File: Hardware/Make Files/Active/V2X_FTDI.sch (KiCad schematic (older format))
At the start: 27 parts, among them P5 USB_u, U12 FT4232H, U14 93C46, X1 12M

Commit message: Saving V1.1 as archive.
We are trying a new architecture where the FTDI can be removed. making a
backup spot
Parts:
- removed C30, C32, C33, C34, C35, C36, C37, C38, C39, C40: 100N, Capacitors_SMD:C_0603, symbol C
- removed C31: 4U7, Capacitors_SMD:C_0805, symbol CP1
- removed FB6: 220, Capacitors_SMD:C_0805, symbol FILTER
- removed P5: USB_u, Connect:USB_Micro-B, symbol USB_OTG
- removed R3: DNS, Resistors_SMD:R_0603, symbol R
- added C?: 4U7, Capacitors_SMD:C_0805, symbol CP1
- added C? (x10): 100N, Capacitors_SMD:C_0603, symbol C
- added FB?: 220, Capacitors_SMD:C_0805, symbol FILTER
- added R?: DNS, Resistors_SMD:R_0603, symbol R
- added R?: 0, Resistors_SMD:R_0603, symbol R
- C1: renamed from C28; Mouse PN (none) -> 810-C1608X7R1E104K
- C2: renamed from C29; Mouse PN (none) -> 963-LMK212B7475KG-T
- FB1: renamed from FB5; Mouse PN (none) -> 810-MPZ1608S221ATA00
- U1: renamed from U12; Mouse PN (none) -> 895-FT4232HL
- renumbered C54 to C14, C55 to C15, R54 to R1, R59 to R2, R60 to R3, R61 to R4, R62 to R5, U14 to U2
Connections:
- net labels added: ACCEL_RXD, ACCEL_TXD, CAN_RXD_FTDI, CAN_TXD, FTDI_DM, FTDI_DP, HUB_PWR_PRT1, PC_RXD, PC_TXD
- net labels removed: 5V0_OUT, ACL_CS, ACL_EN, ACL_INT1, ACL_INT2, ACL_SCK, ACL_SDI, ACL_SDO, GPRS_EN, GPRS_RESET, PB0, PB1, PD0, PD1, PD2, PD3, SIMCARD, UART_RXD, UART_TXD, USB_M, USB_P
- wire segments 64 -> 54
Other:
- note added: "Serial channel for Accelerometer data\n"
- note added: "Serial channel for OBD interface control\n"
- note added: "Serial channel for Power Sequencer control\n"
- note added: "Theory:\nThe hub will activate the FTDI\nas the USB port becomes available\nAlternately, PWRSEQ could control directly"
- note removed: "4V1_EN\nACL_EN_ALT\nOBD-SLEEP\nODB_RESET\nSIM CARD DETECT\nRING INDICATOR FROM GSM\nGSM ENABLE\nGSM RESET\n"
- note removed: "HOST Data Connection"
- note removed: "SCK\nDO\nDI\nCS\nGPIO0\nGPIO1\nGPIO2\nGPIO3"
- moved on the sheet: C14, C15, R1, U1

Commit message: V1.2 mostly done
BOM is integrated and creates mouser orders
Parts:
- removed C14, C15: 18P, Capacitors_SMD:C_0603, symbol C
- removed C2, C?: 4U7, Capacitors_SMD:C_0805, symbol CP1
- removed C? (x10): 100N, Capacitors_SMD:C_0603, symbol C
- removed R3, R4: 10K, Resistors_SMD:R_0603, symbol R
- removed R?: DNS, Resistors_SMD:R_0603, symbol R
- added C10, C11, C12, C13, C2, C4, C5, C6, C7, C8, C9: 100N, Capacitors_SMD:C_0603, symbol C
- added C3: 4U7, Capacitors_SMD:C_0603, symbol C
- added R6: 10K, Resistors_SMD:R_0603, symbol R
- added R7: 22K, Resistors_SMD:R_0603, symbol R
- added R?: 0, Resistors_SMD:R_0603, symbol R
- C1: value 100N -> 4U7; Mouse PN 810-C1608X7R1E104K -> 963-LMK212B7475KG-T
- R1: footprint Resistors_SMD:R_0603 -> (none); Mouse PN (none) -> 71-CRCW0603-12K-E3
- R3: renamed from R?; value 0 -> DNS
- R4: renamed from R2; Mouse PN (none) -> 71-CRCW0603-10K-E3
- R5: value 22K -> 10K; Mouse PN (none) -> 71-CRCW0603-10K-E3
- U2: Mouse PN (none) -> 579-93LC46BISN
- X1: value 12M -> 12MHz; symbol Crystal_Small -> CRYSTAL_SMD; Mouse PN (none) -> 815-AWSCR-12.00CV-T
- gave numbers to parts that had none: 1
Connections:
- net labels added: 3V3_B, SEQ_RXD, SEQ_TXD, ~FTDI_RESET
- net labels removed: 3V3, FTDI_RESET, PC_RXD, PC_TXD
- wire segments 54 -> 53

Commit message: V2X v1.2 sch and bom
Made changes to the schematic to V1.2 (remove FTDI possibly) and
integrade the BOM information into the sch
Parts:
- gave numbers to parts that had none: 1
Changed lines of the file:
@@
 TXD\nRXD\n~RTS\n~CTS\n~DTR\n~DSR\n~DCD\n~RI
 $Comp
-L GND #PWR01
+L GND #PWR16
 U 1 1 55AD7D06
 P 7700 4950
-F 0 "#PWR01" H 7700 4700 50  0001 C CNN
+F 0 "#PWR16" H 7700 4700 50  0001 C CNN
 F 1 "GND" V 7700 4750 50  0000 C CNN
 F 2 "" H 7700 4950 60  0000 C CNN
@@
 $EndComp
 $Comp
-L GND #PWR02
+L GND #PWR17
 U 1 1 55AD7D39
 P 5600 5050
-F 0 "#PWR02" H 5600 4800 50  0001 C CNN
+F 0 "#PWR17" H 5600 4800 50  0001 C CNN
 F 1 "GND" V 5600 4850 50  0000 C CNN
 F 2 "" H 5600 5050 60  0000 C CNN
@@
 $EndComp
 $Comp
-L GND #PWR03
+L GND #PWR11
 U 1 1 55AD8749
 P 1200 3650
-F 0 "#PWR03" H 1200 3400 50  0001 C CNN
+F 0 "#PWR11" H 1200 3400 50  0001 C CNN
 F 1 "GND" H 1200 3500 50  0000 C CNN
 F 2 "" H 1200 3650 60  0000 C CNN
@@
 $EndComp
 $Comp
-L GND #PWR04
+L GND #PWR1
 U 1 1 55AD885E
 P 1700 1250
-F 0 "#PWR04" H 1700 1000 50  0001 C CNN
+F 0 "#PWR1" H 1700 1000 50  0001 C CNN
 F 1 "GND" H 1700 1100 50  0000 C CNN
 F 2 "" H 1700 1250 60  0000 C CNN
@@
 $EndComp
 $Comp
-L GND #PWR05
+L GND #PWR3
 U 1 1 55AD8999
 P 1700 2100
-F 0 "#PWR05" H 1700 1850 50  0001 C CNN
+F 0 "#PWR3" H 1700 1850 50  0001 C CNN
 F 1 "GND" H 1700 1950 50  0000 C CNN
 F 2 "" H 1700 2100 60  0000 C CNN
@@
 $EndComp
 $Comp
-L GND #PWR06
+L GND #PWR5
 U 1 1 55AD8CCE
 P 1050 2850
-F 0 "#PWR06" H 1050 2600 50  0001 C CNN
+F 0 "#PWR5" H 1050 2600 50  0001 C CNN
 F 1 "GND" H 1050 2700 50  0000 C CNN
 F 2 "" H 1050 2850 60  0000 C CNN
@@
 Power Filtering
 $Comp
-L GND #PWR07
+L GND #PWR10
 U 1 1 55AD97DA
 P 5200 3050
-F 0 "#PWR07" H 5200 2800 50  0001 C CNN
+F 0 "#PWR10" H 5200 2800 50  0001 C CNN
 F 1 "GND" V 5200 2850 50  0000 C CNN
 F 2 "" H 5200 3050 60  0000 C CNN
@@
 $EndComp
 $Comp
-L GND #PWR08
+L GND #PWR15
 U 1 1 55AD9B20
 P 5700 3750
-F 0 "#PWR08" H 5700 3500 50  0001 C CNN
+F 0 "#PWR15" H 5700 3500 50  0001 C CNN
 F 1 "GND" H 5700 3600 50  0000 C CNN
 F 2 "" H 5700 3750 60  0000 C CNN
@@
 EECLK
 $Comp
-L GND #PWR09
+L GND #PWR19
 U 1 1 55ADAE78
 P 1550 7500
-F 0 "#PWR09" H 1550 7250 50  0001 C CNN
+F 0 "#PWR19" H 1550 7250 50  0001 C CNN
 F 1 "GND" V 1550 7300 50  0000 C CNN
 F 2 "" H 1550 7500 60  0000 C CNN
@@
 FTDI Device Configuration EEPROM
 $Comp
-L GND #PWR010
+L GND #PWR2
 U 1 1 55ADBFB3
 P 1950 1250
-F 0 "#PWR010" H 1950 1000 50  0001 C CNN
+F 0 "#PWR2" H 1950 1000 50  0001 C CNN
 F 1 "GND" H 1950 1100 50  0000 C CNN
 F 2 "" H 1950 1250 60  0000 C CNN
@@
 $EndComp
 $Comp
-L GND #PWR011
+L GND #PWR4
 U 1 1 55ADBFF1
 P 1950 2100
-F 0 "#PWR011" H 1950 1850 50  0001 C CNN
+F 0 "#PWR4" H 1950 1850 50  0001 C CNN
 F 1 "GND" H 1950 1950 50  0000 C CNN
 F 2 "" H 1950 2100 60  0000 C CNN
@@
 $EndComp
 $Comp
-L GND #PWR012
+L GND #PWR12
 U 1 1 55ADC2B9
 P 1500 3650
-F 0 "#PWR012" H 1500 3400 50  0001 C CNN
+F 0 "#PWR12" H 1500 3400 50  0001 C CNN
 F 1 "GND" H 1500 3500 50  0000 C CNN
 F 2 "" H 1500 3650 60  0000 C CNN
@@
 $EndComp
 $Comp
-L GND #PWR013
+L GND #PWR6
 U 1 1 55ADC2C5
 P 1350 2850
-F 0 "#PWR013" H 1350 2600 50  0001 C CNN
+F 0 "#PWR6" H 1350 2600 50  0001 C CNN
 F 1 "GND" H 1350 2700 50  0000 C CNN
 F 2 "" H 1350 2850 60  0000 C CNN
@@
 $EndComp
 $Comp
-L GND #PWR014
+L GND #PWR13
 U 1 1 55ADC34F
 P 1800 3650
-F 0 "#PWR014" H 1800 3400 50  0001 C CNN
+F 0 "#PWR13" H 1800 3400 50  0001 C CNN
 F 1 "GND" H 1800 3500 50  0000 C CNN
 F 2 "" H 1800 3650 60  0000 C CNN
@@
 $EndComp
 $Comp
-L GND #PWR015
+L GND #PWR7
 U 1 1 55ADC35B
 P 1650 2850
-F 0 "#PWR015" H 1650 2600 50  0001 C CNN
+F 0 "#PWR7" H 1650 2600 50  0001 C CNN
 F 1 "GND" H 1650 2700 50  0000 C CNN
 F 2 "" H 1650 2850 60  0000 C CNN
@@
 $EndComp
 $Comp
-L GND #PWR016
+L GND #PWR8
 U 1 1 55ADC37F
 P 1950 2850
-F 0 "#PWR016" H 1950 2600 50  0001 C CNN
+F 0 "#PWR8" H 1950 2600 50  0001 C CNN
 F 1 "GND" H 1950 2700 50  0000 C CNN
 F 2 "" H 1950 2850 60  0000 C CNN
@@
 $EndComp
 $Comp
-L GND #PWR017
+L GND #PWR14
 U 1 1 55ADC373
 P 2100 3650
-F 0 "#PWR017" H 2100 3400 50  0001 C CNN
+F 0 "#PWR14" H 2100 3400 50  0001 C CNN
 F 1 "GND" H 2100 3500 50  0000 C CNN
 F 2 "" H 2100 3650 60  0000 C CNN
@@
 $EndComp
 $Comp
-L GND #PWR018
+L GND #PWR9
 U 1 1 55ADC68C
 P 2250 2850
-F 0 "#PWR018" H 2250 2600 50  0001 C CNN
+F 0 "#PWR9" H 2250 2600 50  0001 C CNN
 F 1 "GND" H 2250 2700 50  0000 C CNN
 F 2 "" H 2250 2850 60  0000 C CNN
@@
 3V3_B
 $Comp
-L R R?
+L R R2
 U 1 1 56090D92
 P 4900 3150
-F 0 "R?" V 4980 3150 50  0000 C CNN
+F 0 "R2" V 4980 3150 50  0000 C CNN
 F 1 "0" V 4900 3150 50  0000 C CNN
 F 2 "Resistors_SMD:R_0603" V 4830 3150 30  0001 C CNN
@@
 $EndComp
 $Comp
-L GND #PWR019
+L GND #PWR18
 U 1 1 55B7E844
 P 5350 6950
-F 0 "#PWR019" H 5350 6700 50  0001 C CNN
+F 0 "#PWR18" H 5350 6700 50  0001 C CNN
 F 1 "GND" H 5350 6800 50  0000 C CNN
 F 2 "" H 5350 6950 60  0000 C CNN

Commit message: Split V2X in 2 boards, layout of SIM pcb done
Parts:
- C1, C3: footprint Capacitors_SMD:C_0603 -> Custom Parts:C_0805_SM
- C10, C11, C12, C13, C2, C4, C5, C6, C7, C8, C9: footprint Capacitors_SMD:C_0603 -> Custom Parts:C_0603_SM
- FB1, FB2: footprint Capacitors_SMD:C_0805 -> Custom Parts:R_0603_sm
- R1: footprint (none) -> Custom Parts:R_0603_sm
- R2, R3, R4, R5, R6, R7: footprint Resistors_SMD:R_0603 -> Custom Parts:R_0603_sm
- X1: footprint Custom Parts:ABLS7M -> Custom Parts:AWSCR
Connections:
- net labels added: FT_CLKN
- net labels removed: FT_CLK_M
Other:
- note removed: "Theory:\nThe hub will activate the FTDI\nas the USB port becomes available\nAlternately, PWRSEQ could control directly"

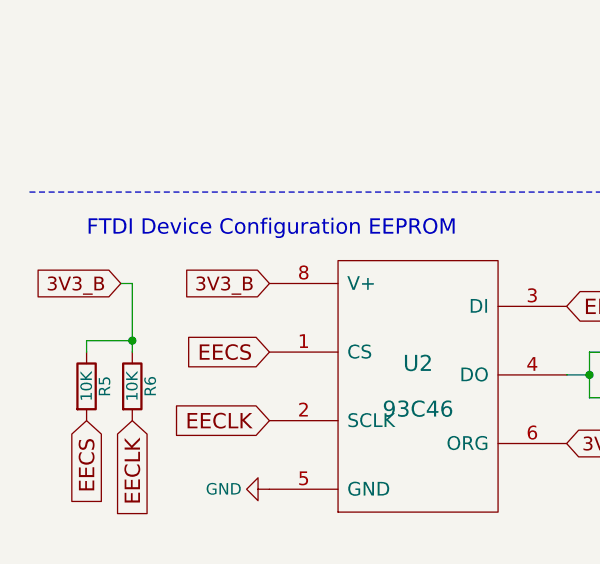
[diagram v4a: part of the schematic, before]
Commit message: Build pass of main V2X board
ready to verify
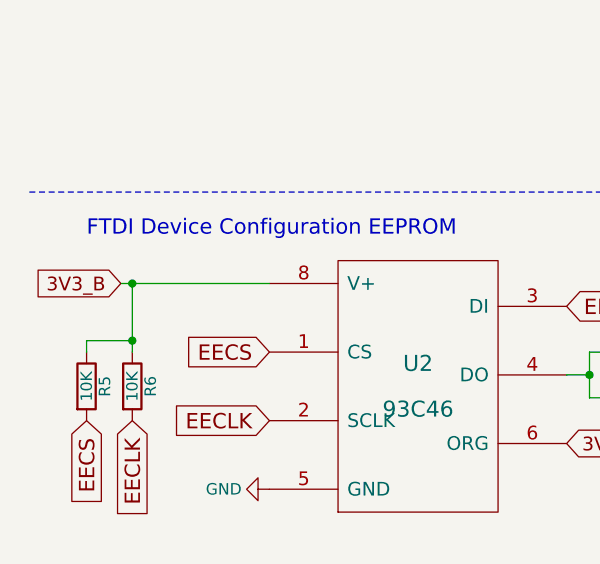
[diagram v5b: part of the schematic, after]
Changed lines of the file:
@@
 	1    0    0    -1
 $EndComp
-Text GLabel 1550 6900 0    67   Input ~ 0
-EECS
 Text GLabel 3300 7100 2    67   Input ~ 0
 EEDATA
@@
 	2650 4000 2650 500
 Wire Wire Line
-	900  6600 950  6600
+	900  6600 1550 6600
 Wire Notes Line
 	500  4000 2650 4000
@@
 Text GLabel 900  6600 0    60   Input ~ 0
 3V3_B
-Text GLabel 1550 6600 0    60   Input ~ 0
-3V3_B
 Text GLabel 2850 7300 2    60   Input ~ 0
 3V3_B
@@
 	-1   0    0    -1
 $EndComp
+Text GLabel 1550 6900 0    67   Input ~ 0
+EECS
+Connection ~ 950  6600
 $EndSCHEMATC

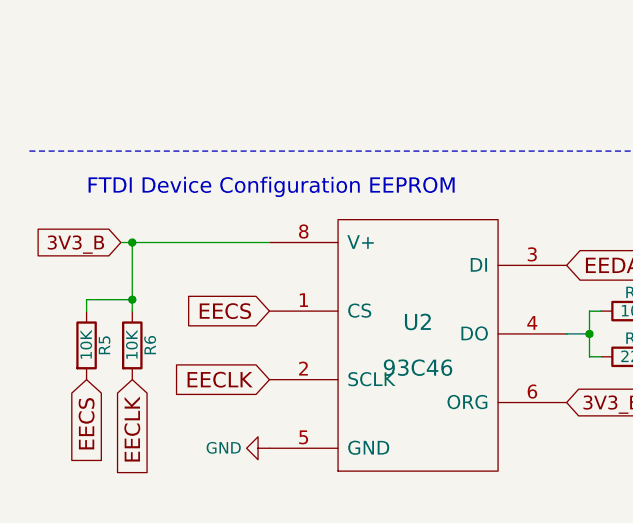
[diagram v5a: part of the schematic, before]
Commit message: Project rework
Split the Main and GSM boards into separate projects, redesigned Main
board after flaws were found.
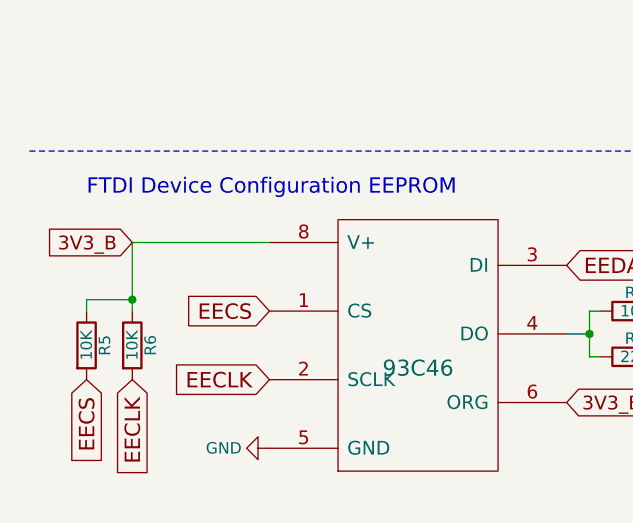
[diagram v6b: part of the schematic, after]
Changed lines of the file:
@@
 $Descr A4 11693 8268
 encoding utf-8
-Sheet 2 8
+Sheet 2 7
 Title "V2X - Open source RVI over SMS daughter card"
 Date "2015-07-17"
@@
 U 1 1 55ADA8E8
 P 2200 7050
-F 0 "U2" H 2200 7150 70  0000 C CNN
+F 0 "U2" H 2200 7150 70  0001 C CNN
 F 1 "93C46" H 2200 6950 70  0000 C CNN
 F 2 "Housings_SOIC:SOIC-8_3.9x4.9mm_Pitch1.27mm" H 2200 7050 60  0001 C CNN
@@
 Wire Notes Line
 	2650 4000 2650 500
-Wire Wire Line
-	900  6600 1550 6600
 Wire Notes Line
 	500  4000 2650 4000
@@
 	0    -1   -1   0
 $EndComp
-Text GLabel 900  6600 0    60   Input ~ 0
+Text GLabel 950  6600 0    60   Input ~ 0
 3V3_B
 Text GLabel 2850 7300 2    60   Input ~ 0
@@
 Text GLabel 1550 6900 0    67   Input ~ 0
 EECS
-Connection ~ 950  6600
+Wire Wire Line
+	1550 6600 950  6600
 $EndSCHEMATC

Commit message: No Rpi Backpower fix
added a USB-A to the board to power the HOST. fixed LED labeling.
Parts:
- U2: symbol 9346 -> 9346_noVcc
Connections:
- wire segments 53 -> 56
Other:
- moved on the sheet: R1, R2, R3, U1
